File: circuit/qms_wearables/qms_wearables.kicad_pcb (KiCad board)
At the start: 2 copper layers, 3 parts, among them P1 SEN-11574, U1 ESP32-DEVKIT-V1, U2 module_mpu6050

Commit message: wip: First draft complete kiosk circuit.
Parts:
- added BT1: BK-18650-PC4, BK-18650-PC4:BAT_BK-18650-PC4, F.Cu at (144.8, 68.6)
- added P2: PWM VIBRATION MOTOR, SEN_11574:XDCR_SEN-11574, F.Cu at (162.6, 129.5)
- added S1: EG1218, DPST_slide_switch:SW_EG1218, F.Cu at (185.5, 134.6)
- moved P1 56.7 mm to (162.6, 142.2)
- moved U1 33.8 mm to (119.4, 119.4), turned to 180 degrees
- moved U2 14.5 mm to (158.1, 115.7)
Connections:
- U1 pad 15: unconnected-(U1-D23-Pad15) -> Net-(P2-SIGNAL)
- U1 pad 17: Net-(P1-SIGNAL) -> unconnected-(U1-VP-Pad17)
- U1 pad 19: unconnected-(U1-D34-Pad19) -> Net-(P1-SIGNAL)
- U1 pad 30: +5V -> Net-(U1-VIN)
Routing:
- net GND: track 0.00 -> 566.9 mm
- net Net-(P1-SIGNAL): track 0.00 -> 361.3 mm
- net Net-(BT1-Pad1+): track 0.00 -> 131.4 mm
- net +3.3V: track 0.00 -> 108.3 mm
- net Net-(P2-SIGNAL): track 0.00 -> 95.3 mm
- net Net-(U1-VIN): track 0.00 -> 85.8 mm
- net Net-(BT1-Pad2-): track 0.00 -> 62.5 mm
- net Net-(U1-D22): track 0.00 -> 28.8 mm
- net Net-(U1-D21): track 0.00 -> 27.7 mm
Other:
- board outline added: 139.7 x 124.5 mm

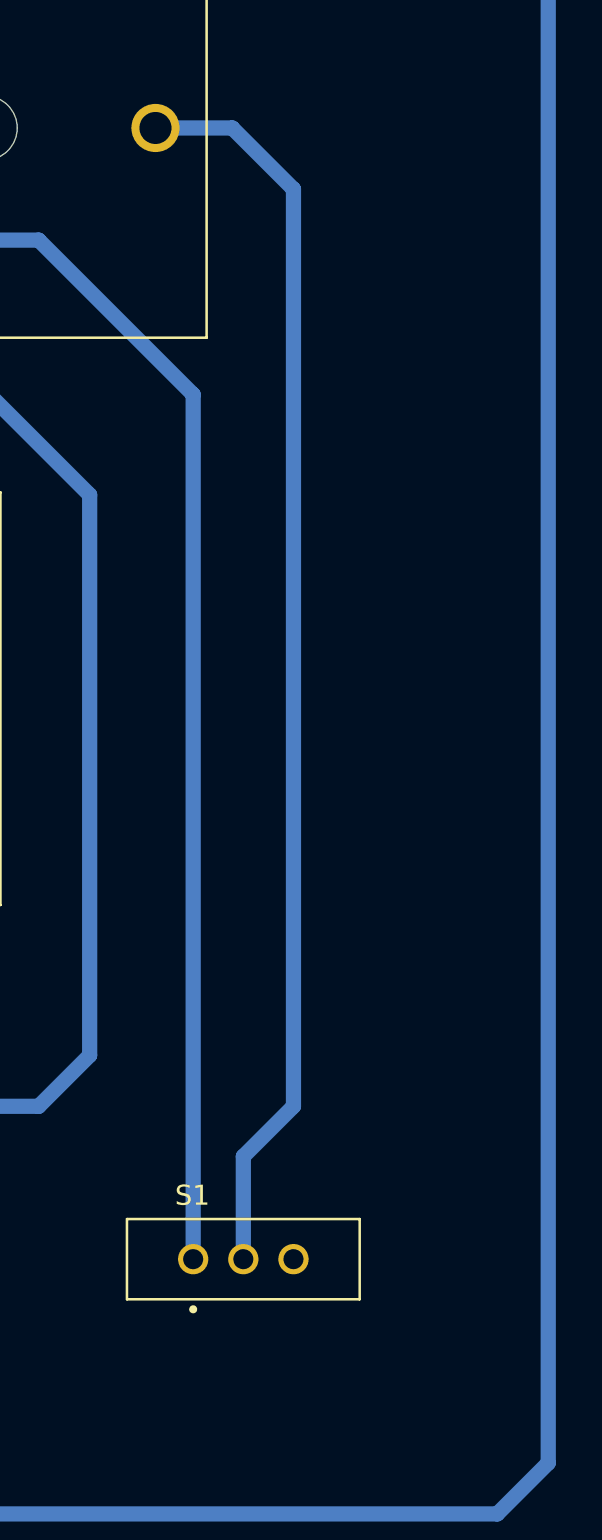
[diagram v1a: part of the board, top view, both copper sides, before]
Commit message: wip: First draft complete wearable circuit schematic and pcb with adding 2x battery, DC vibration motor module.
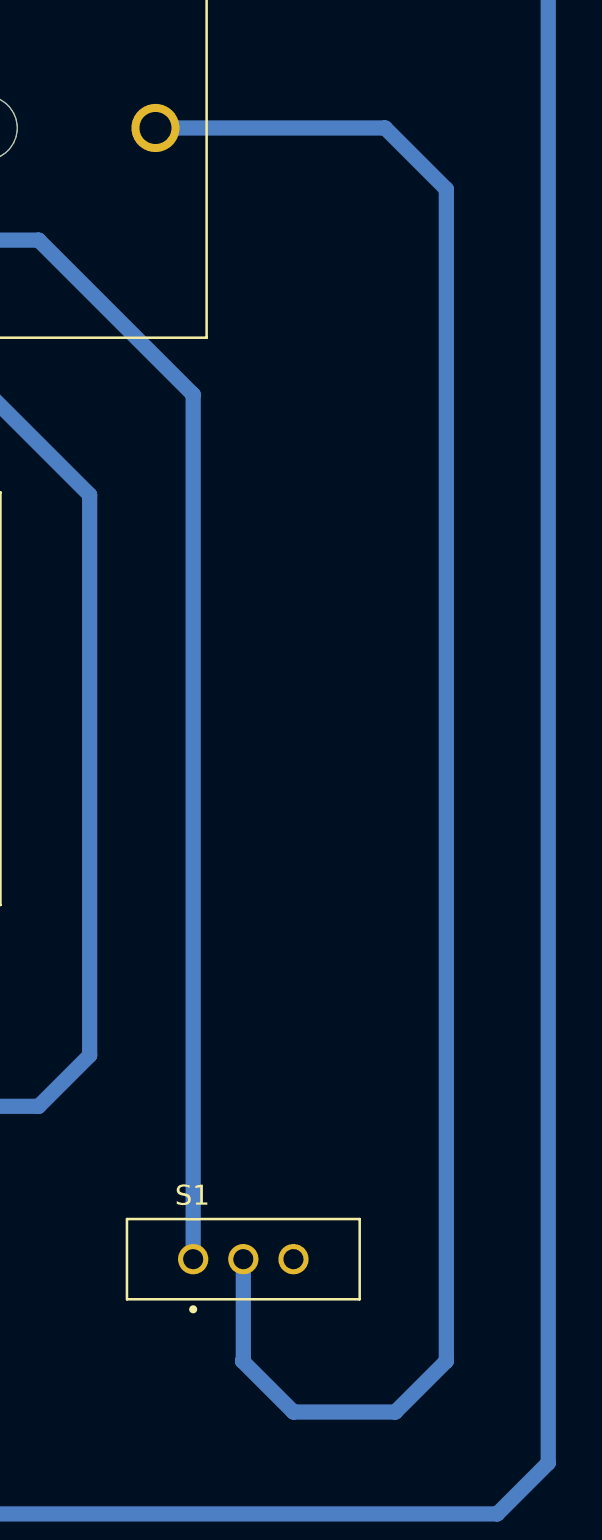
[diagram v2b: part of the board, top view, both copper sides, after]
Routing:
- net Net-(BT1-Pad2-): track 62.5 -> 91.5 mm
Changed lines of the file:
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@@
 	)
 	(segment
-		(start 187.96 81.28)
-		(end 184.91 78.23)
+		(start 192.53 78.23)
+		(end 181.08 78.23)
+		(width 0.76)
+		(layer "B.Cu")
+		(net 32)
+	)
+	(segment
+		(start 193.04 142.24)
+		(end 195.58 139.7)
+		(width 0.76)
+		(layer "B.Cu")
+		(net 32)
+	)
+	(segment
+		(start 187.96 142.24)
+		(end 193.04 142.24)
+		(width 0.76)
+		(layer "B.Cu")
+		(net 32)
+	)
+	(segment
+		(start 185.42 139.7)
+		(end 187.96 142.24)
+		(width 0.76)
+		(layer "B.Cu")
+		(net 32)
+	)
+	(segment
+		(start 195.58 81.28)
+		(end 192.53 78.23)
+		(width 0.76)
+		(layer "B.Cu")
+		(net 32)
+	)
+	(segment
+		(start 195.58 139.7)
+		(end 195.58 81.28)
+		(width 0.76)
+		(layer "B.Cu")
+		(net 32)
+	)
+	(segment
+		(start 185.46 139.66)
+		(end 185.42 139.7)
 		(width 0.76)
 		(layer "B.Cu")
@@
 	(segment
 		(start 185.46 134.62)
-		(end 185.46 129.5)
+		(end 185.46 139.66)
 		(width 0.76)
 		(layer "B.Cu")
-		(net 32)
-	)
-	(segment
-		(start 184.91 78.23)
-		(end 181.08 78.23)
-		(width 0.76)
-		(layer "B.Cu")
-		(net 32)
-	)
-	(segment
-		(start 187.96 127)
-		(end 187.96 81.28)
-		(width 0.76)
-		(layer "B.Cu")
-		(net 32)
-	)
-	(segment
-		(start 185.46 129.5)
-		(end 187.96 127)
-		(width 0.76)
-		(layer "B.Cu")

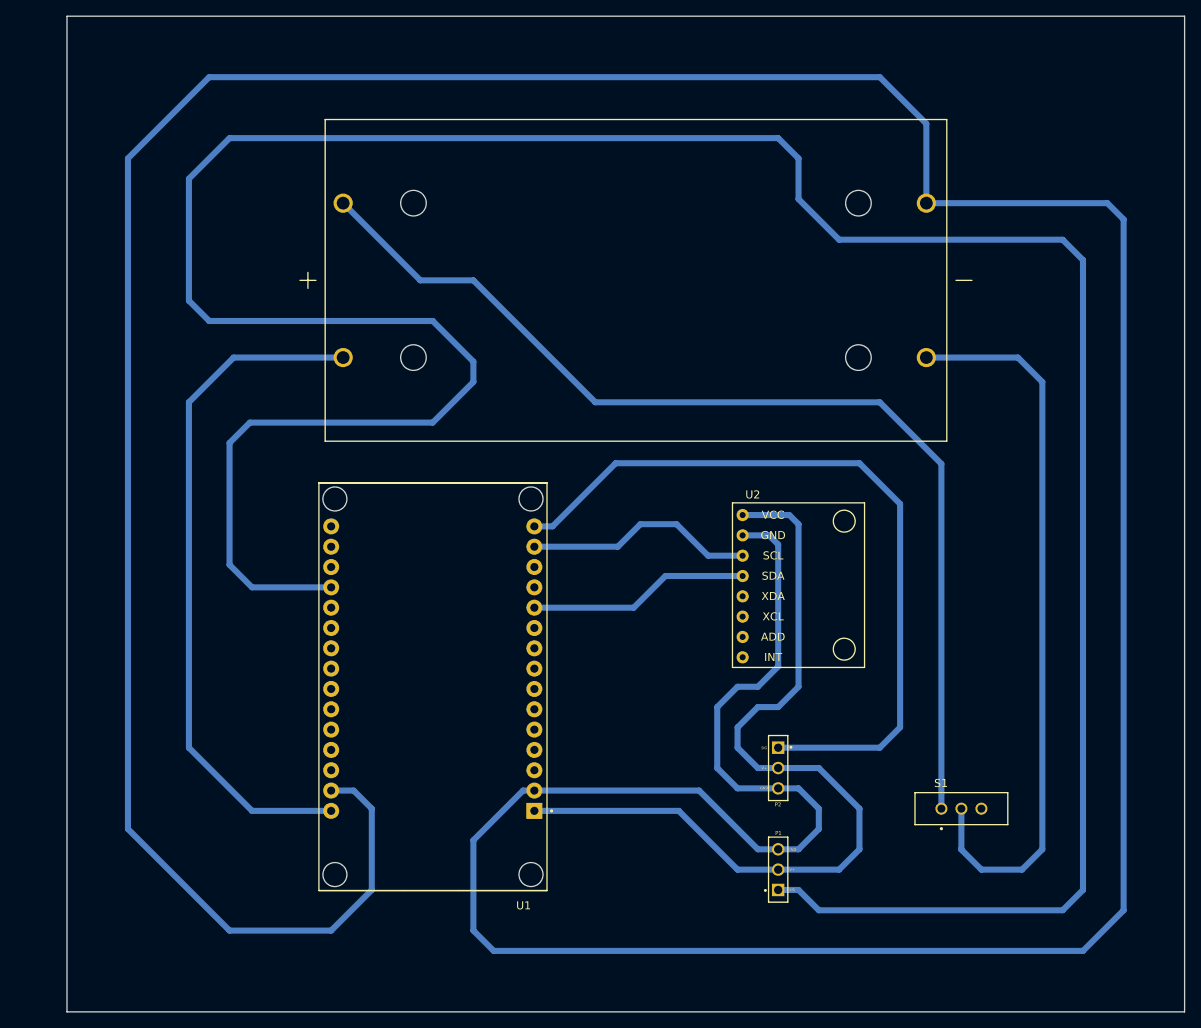
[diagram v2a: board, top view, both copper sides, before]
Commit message: wip: Second draft with replacing the schematic and footprint of vibration motor module
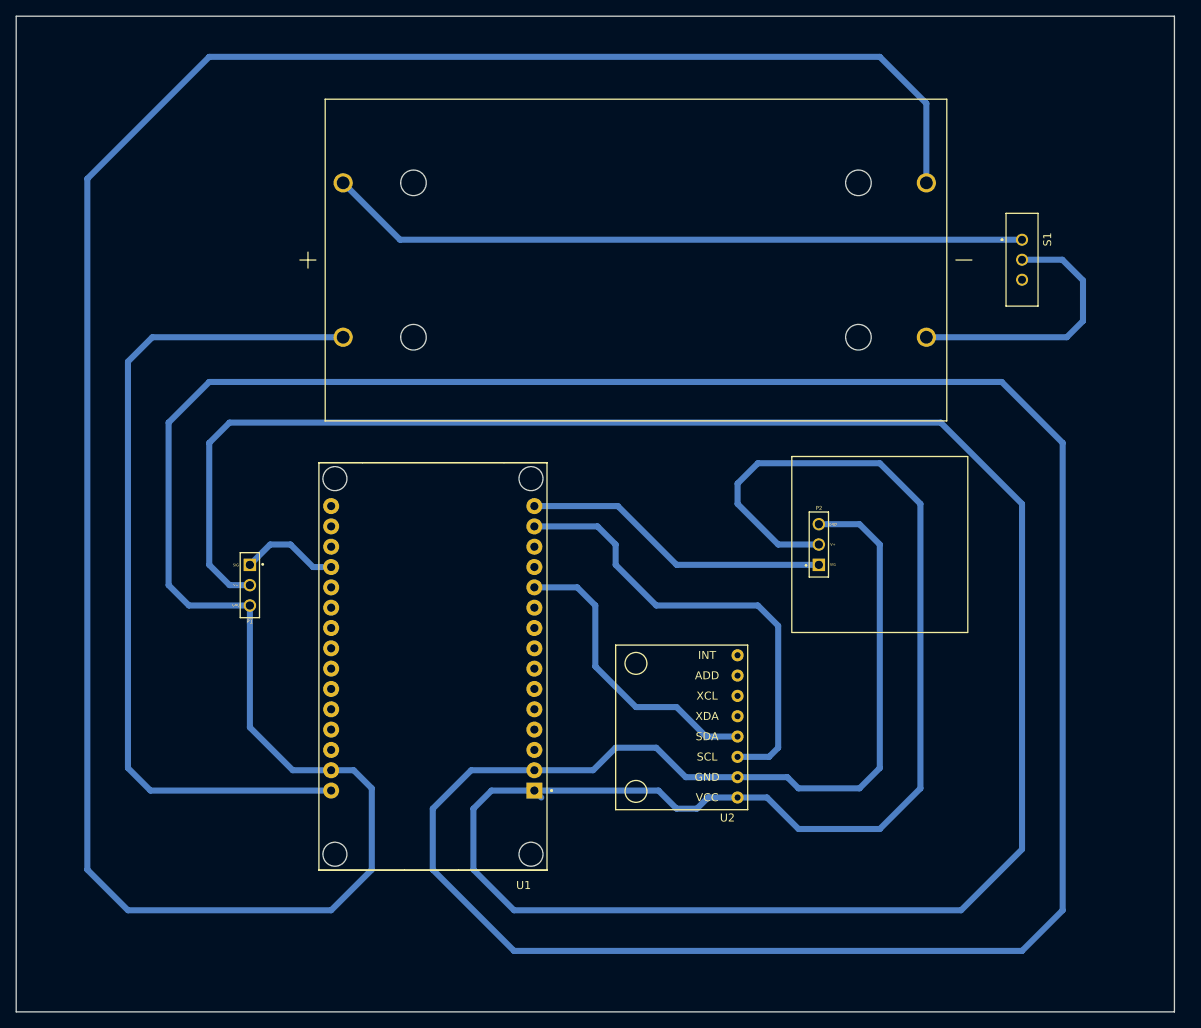
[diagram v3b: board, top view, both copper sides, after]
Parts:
- P2: value PWM VIBRATION MOTOR -> Vibration Motor Module; footprint SEN_11574:XDCR_SEN-11574 -> Vibration_Motor_Module:XDCR_Vibration_Motor_Module
- moved P1 75.0 mm to (96.5, 106.7), turned to 180 degrees
- moved S1 69.0 mm to (193.0, 66.0), turned to -90 degrees
- moved P2 30.7 mm to (175.3, 101.6), turned to 0 degrees
- moved BT1 2.54 mm to (144.8, 66.0)
- moved U1 2.54 mm to (119.4, 116.8)
- moved U2 0.68 mm to (157.5, 115.4), turned to 180 degrees
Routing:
- net Net-(P1-SIGNAL): track 361.3 -> 12.4 mm
- net +3.3V: track 108.3 -> 392.6 mm
- net GND: track 566.9 -> 691.9 mm
- net Net-(BT1-Pad2-): track 91.5 -> 34.2 mm
- net Net-(P2-SIGNAL): track 95.3 -> 38.6 mm
- net Net-(BT1-Pad1+): track 131.4 -> 87.8 mm
- net Net-(U1-D22): track 28.8 -> 57.9 mm
- net Net-(U1-VIN): track 85.8 -> 105.5 mm
- net Net-(U1-D21): track 27.7 -> 37.6 mm
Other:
- board size 139.7 x 124.5 mm -> 144.8 x 124.5 mm

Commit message: wip: Third draft with reducing size of the edge cuts in wearables pcb as smaller as possible
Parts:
- moved S1 99.1 mm to (94.0, 63.5)
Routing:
- net Net-(BT1-Pad1+): track 87.8 -> 16.1 mm
- net Net-(BT1-Pad2-): track 34.2 -> 94.4 mm
- net GND: track 691.9 -> 653.7 mm
- net +3.3V: track 392.6 -> 369.5 mm
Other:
- board size 144.8 x 124.5 mm -> 124.5 x 116.8 mm

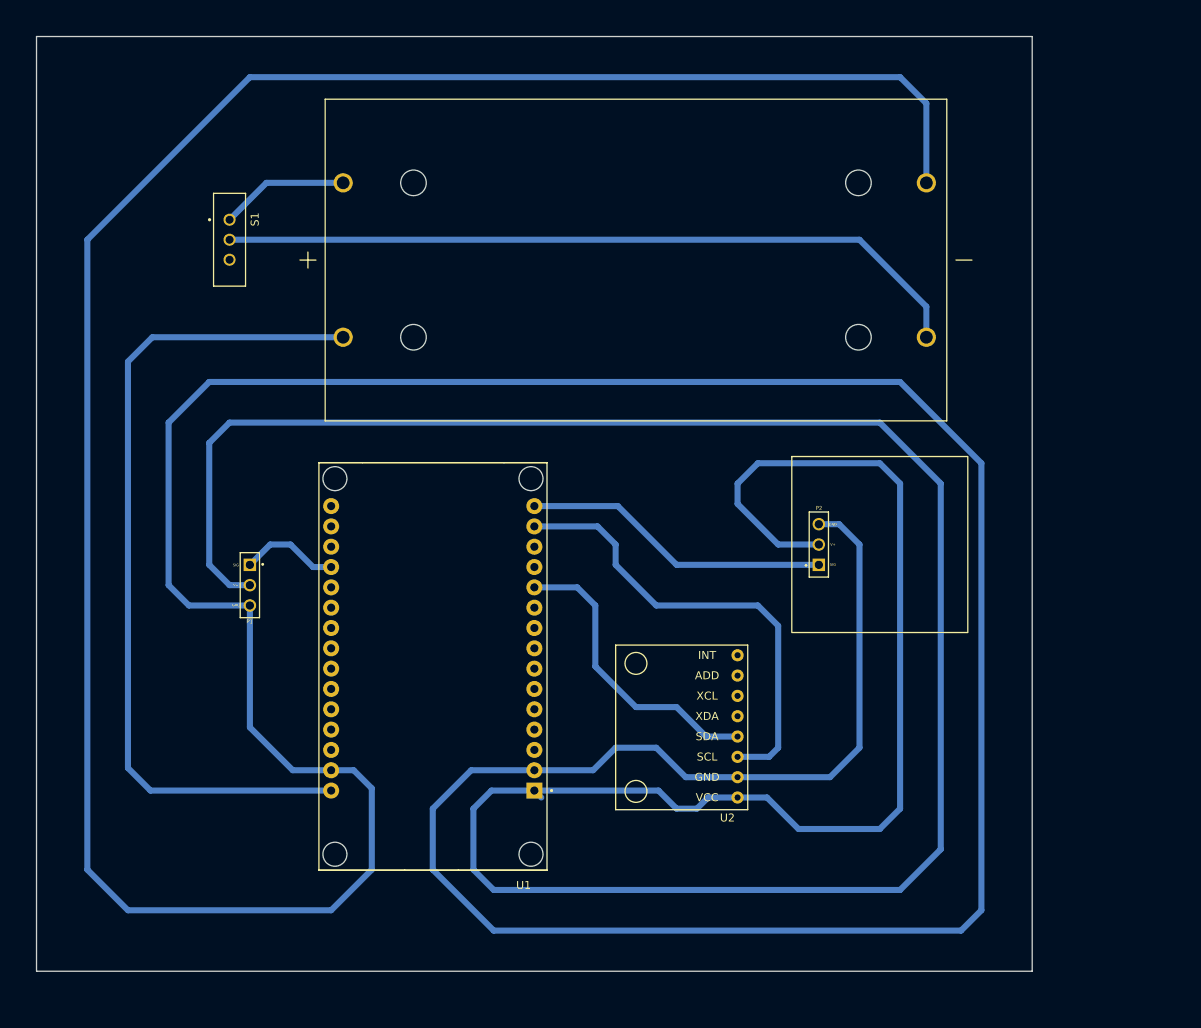
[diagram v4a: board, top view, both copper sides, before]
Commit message: wip: Fourth draft with replacing the DPDT Slide Switch and 2 Cell battery footprint and schematic circuit.
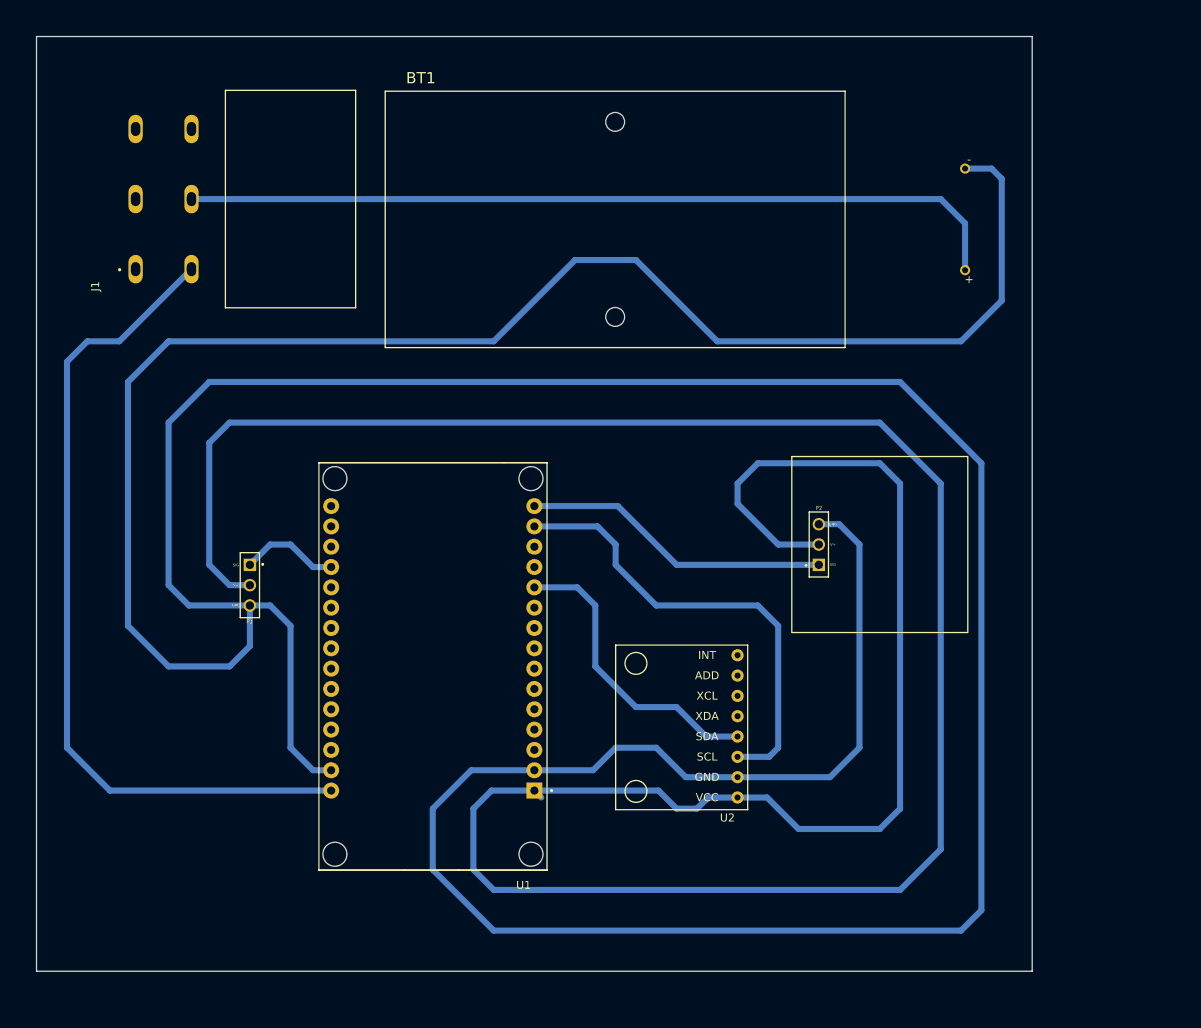
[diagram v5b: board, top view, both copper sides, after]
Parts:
- removed S1: EG1218, DPST_slide_switch:SW_EG1218
- added J1: EPS4PC3, DPDT-SLIDESWITCH-6PINS:SWITCHCRAFT_EPS4PC3, F.Cu at (101.6, 58.4)
- BT1: value BK-18650-PC4 -> BA2AAW; footprint BK-18650-PC4:BAT_BK-18650-PC4 -> BATTERY-2CELLS-2WIRES:BAT_BA2AAW
- moved BT1 5.71 mm to (142.2, 61.0)
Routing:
- net Net-(BT1-Pad+): track 0.00 -> 103.8 mm
- net Net-(BT1-Pad2-): track 94.4 -> 0.00 mm
- net GND: track 653.7 -> 590.6 mm
- net Net-(BT1-Pad1+): track 16.1 -> 0.00 mm
- net Net-(U1-VIN): track 105.5 -> 103.8 mm

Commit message: wip: Draft for changing the pcb traces size from 0.762mm (T30) to 0.508mm(T20).
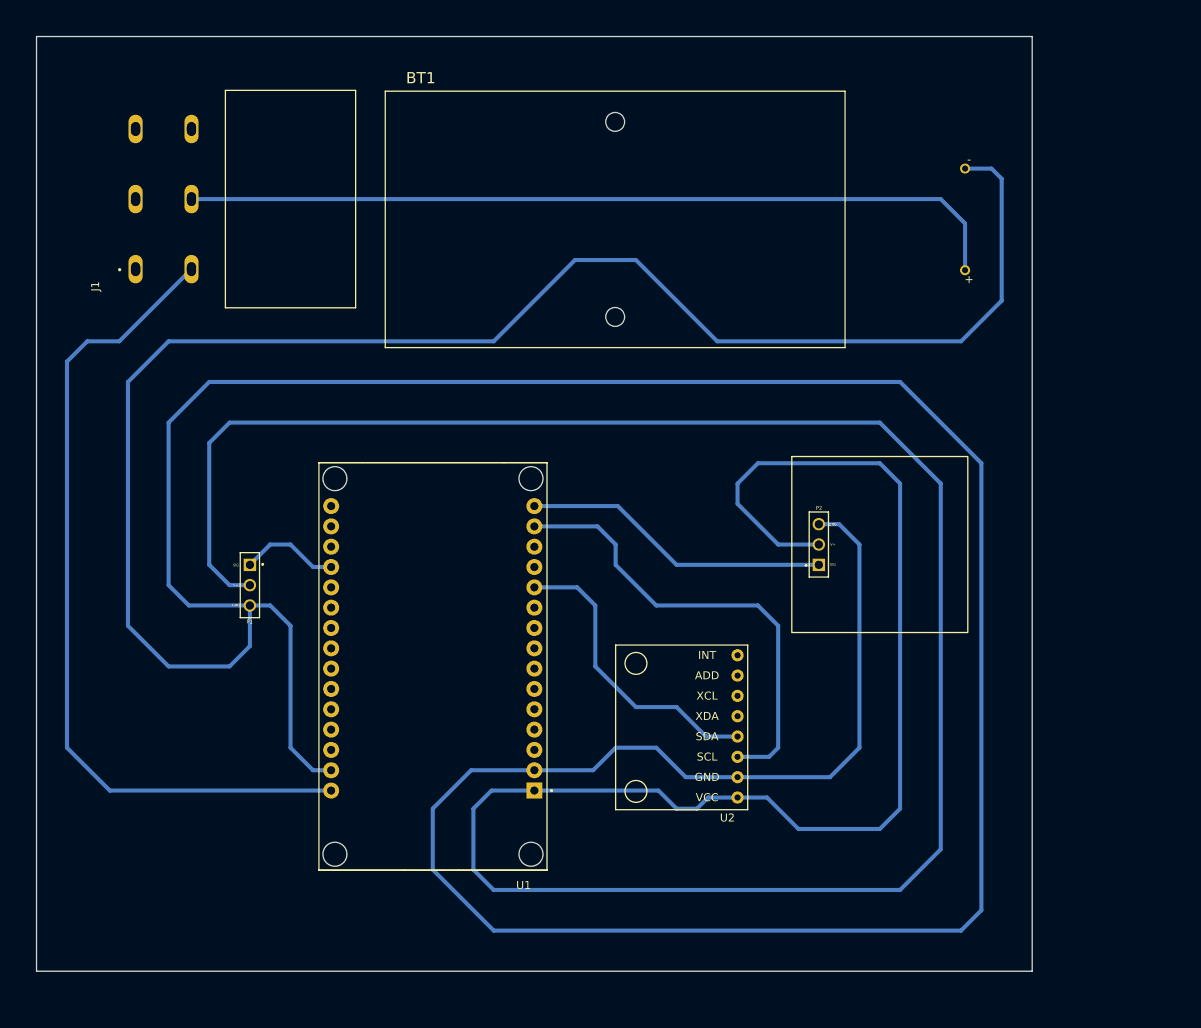
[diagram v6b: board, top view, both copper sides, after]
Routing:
- net +3.3V: track 369.5 -> 368.3 mm
